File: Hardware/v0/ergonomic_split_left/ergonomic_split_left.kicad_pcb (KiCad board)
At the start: 2 copper layers, 189.3 x 173.4 mm, 96 parts, among them J1 USB_C_Receptacle_USB2.0, J2 Right_Interface, J3 Conn_01x02_Male, J5 Conn_02x03_Odd_Even, SW1 SW_Push, SW10 L31, SW11 L41, SW12 L51, SW13 L02, SW14 L12, SW15 L22, SW16 L32, SW17 L42, SW18 L52, SW19 L03, SW2 L00, SW20 L13, SW21 L23, SW22 L33, SW23 L43, SW24 L53, SW25 L04, SW26 L14, SW27 L24, SW28 L34, SW29 L44, SW3 L10, SW30 L54, SW31 L05, SW32 L15, SW33 L25, SW34 L35, SW35 L55, SW36 L16, SW37 L36, SW38 L56, SW39 L06, SW4 L20, SW40 L_Encoder, SW5 L30, SW6 L40, SW7 L01, SW8 L11, SW9 L21, U1 SRV05-4, U2 PCAL9555AHF, U6 ATmega32U4-AU, U9 TCR2EF33, X2 KC2016K

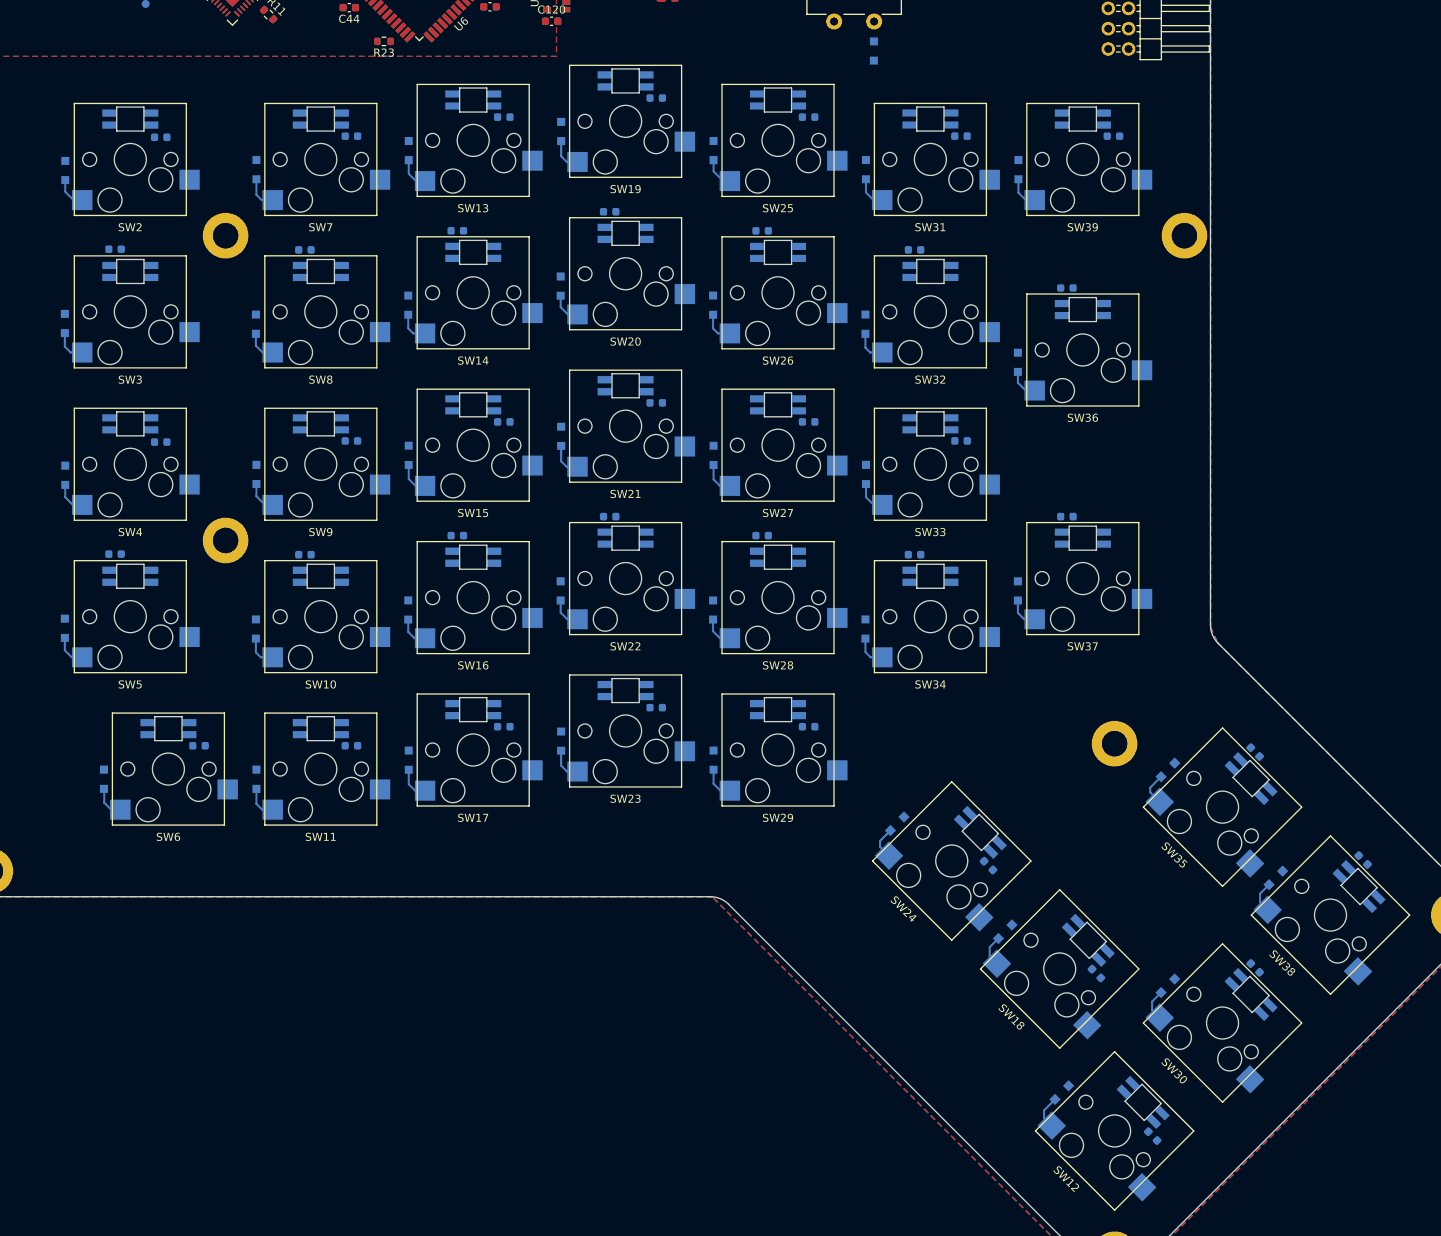
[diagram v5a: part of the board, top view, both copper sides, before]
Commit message: Switch matrix and LEDs prelim routing
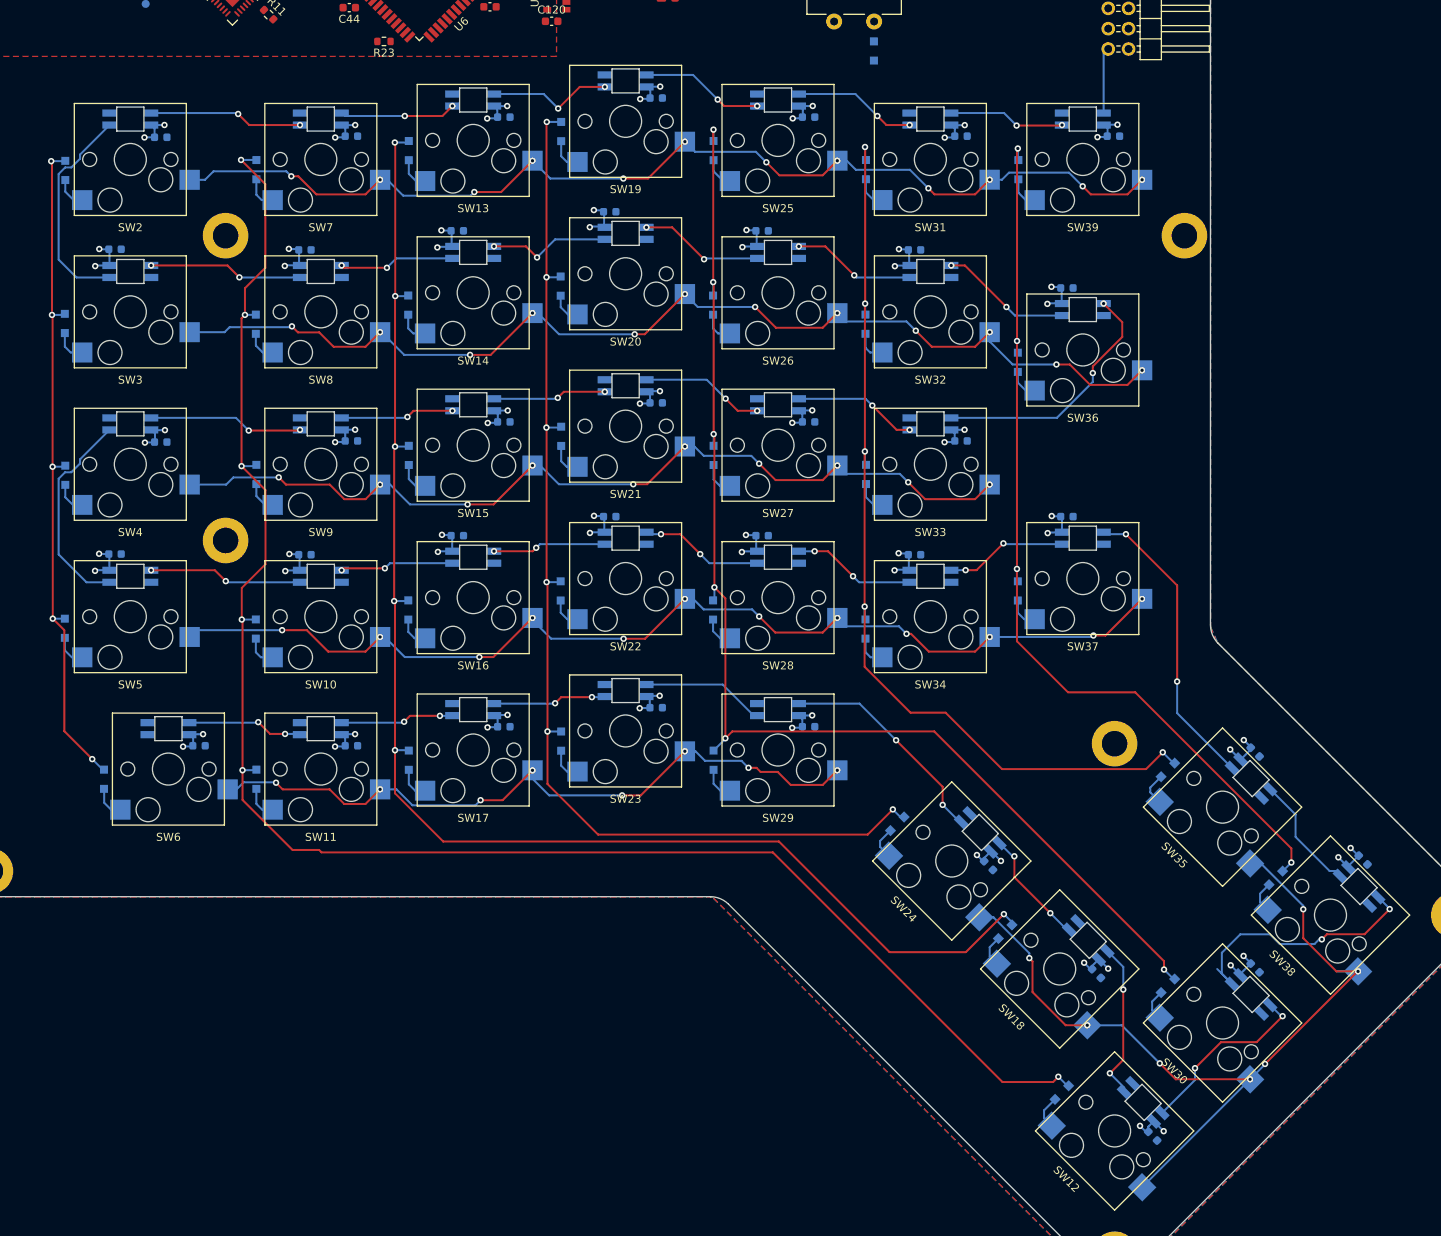
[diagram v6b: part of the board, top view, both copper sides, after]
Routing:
- net /IO Expander/COL[1]: track 0.00 -> 212.3 mm, vias 0 -> 6
- net +5V: track 0.00 -> 179.9 mm, vias 0 -> 76
- net /IO Expander/COL[2]: track 0.00 -> 178.3 mm, vias 0 -> 6
- net /IO Expander/COL[4]: track 0.00 -> 155.1 mm, vias 0 -> 6
- net /IO Expander/COL[3]: track 0.00 -> 140.7 mm, vias 0 -> 6
- net /IO Expander/ROW[1]: track 0.00 -> 136.9 mm, vias 0 -> 12
- net /IO Expander/ROW[3]: track 0.00 -> 134.6 mm, vias 0 -> 12
- net /IO Expander/ROW[0]: track 0.00 -> 134.2 mm, vias 0 -> 12
- net /IO Expander/COL[5]: track 0.00 -> 116.9 mm, vias 0 -> 5
- net /IO Expander/COL[6]: track 0.00 -> 114.5 mm, vias 0 -> 4
- net /IO Expander/ROW[2]: track 0.00 -> 113.2 mm, vias 0 -> 10
- net /IO Expander/ROW[5]: track 0.00 -> 107.2 mm, vias 0 -> 7
- net /IO Expander/ROW[4]: track 0.00 -> 87.8 mm, vias 0 -> 8
- net /IO Expander/COL[0]: track 0.00 -> 85.5 mm, vias 0 -> 5
- net /Switch Matrix/RGB_L55: track 0.00 -> 37.6 mm, vias 0 -> 2
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
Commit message: Prelim routing done
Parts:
- FB1, FB2, R1, R2, R22: moved to B.Cu
- moved SW1 59.8 mm to (99.0, 63.5), turned to 180 degrees
- moved R22 54.4 mm to (100.3, 66.2), turned to 0 degrees
- moved D194 50.1 mm to (140.4, 58.6), turned to 90 degrees
- moved R3 48.5 mm to (138.8, 58.6), turned to 270 degrees
- moved H5 22.0 mm to (168.5, 58.8)
- moved FB2 16.7 mm to (149.3, 62.0)
- moved FB1 5.84 mm to (162.0, 62.4)
- moved R1 5.00 mm to (148.6, 59.0), turned to 0 degrees
- moved TP2 4.91 mm to (92.2, 65.9)
- moved R2 4.77 mm to (158.6, 64.6)
- moved R5 4.49 mm to (149.4, 63.7)
- moved U1 4.37 mm to (155.7, 64.8), turned to 0 degrees
- moved J1 4.03 mm to (158.5, 61.7)
- moved C2 3.83 mm to (159.2, 63.7), turned to 0 degrees
- moved L1 3.73 mm to (153.5, 64.5)
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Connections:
- U1 pad 3: /USB_UPSTREAM/CD+ -> /USB_UPSTREAM/CD-
- U1 pad 4: /USB_UPSTREAM/CD- -> /USB_UPSTREAM/CD+
- U6 pad 38: /Switch Matrix/ENCODER_B_L -> /Right Interface/ENCODER_B_R
- U6 pad 39: /Switch Matrix/ENCODER_A_L -> /Right Interface/ENCODER_A_R
- U6 pad 40: /Right Interface/ENCODER_B_R -> /Switch Matrix/ENCODER_A_L
- U6 pad 41: /Right Interface/ENCODER_A_R -> /Switch Matrix/ENCODER_B_L
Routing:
- net /IO Expander/ROW[5]: track 107.2 -> 345.4 mm, vias 7 -> 11
- net /IO Expander/ROW[4]: track 87.8 -> 225.8 mm, vias 8 -> 10
- net /Switch Matrix/RGB_DIN: track 0.00 -> 130.9 mm, vias 0 -> 3
- net /IO Expander/SCL: track 0.00 -> 129.3 mm, vias 0 -> 1
- net /IO Expander/SDA: track 0.00 -> 124.9 mm, vias 0 -> 1
- net /IO Expander/ROW[3]: track 134.6 -> 256.3 mm, vias 12 -> 14
- net /IO Expander/COL[6]: track 114.5 -> 227.0 mm, vias 4 -> 8
- net /IO Expander/ROW[2]: track 113.2 -> 220.7 mm, vias 10 -> 12
- net /IO Expander/ROW[1]: track 136.9 -> 229.3 mm, vias 12 -> 14
- net /Right Interface/ENCODER_B_R: track 0.00 -> 89.0 mm, vias 0 -> 1
- net /IO Expander/COL[5]: track 116.9 -> 202.6 mm, vias 5 -> 8
- net /Right Interface/ENCODER_A_R: track 0.00 -> 85.5 mm, vias 0 -> 1
- net /IO Expander/ROW[6]: track 0.00 -> 84.5 mm, vias 0 -> 3
- net /IO Expander/ROW[0]: track 134.2 -> 209.9 mm, vias 12 -> 14
- net /IO Expander/COL[4]: track 155.1 -> 220.9 mm, vias 6 -> 8
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
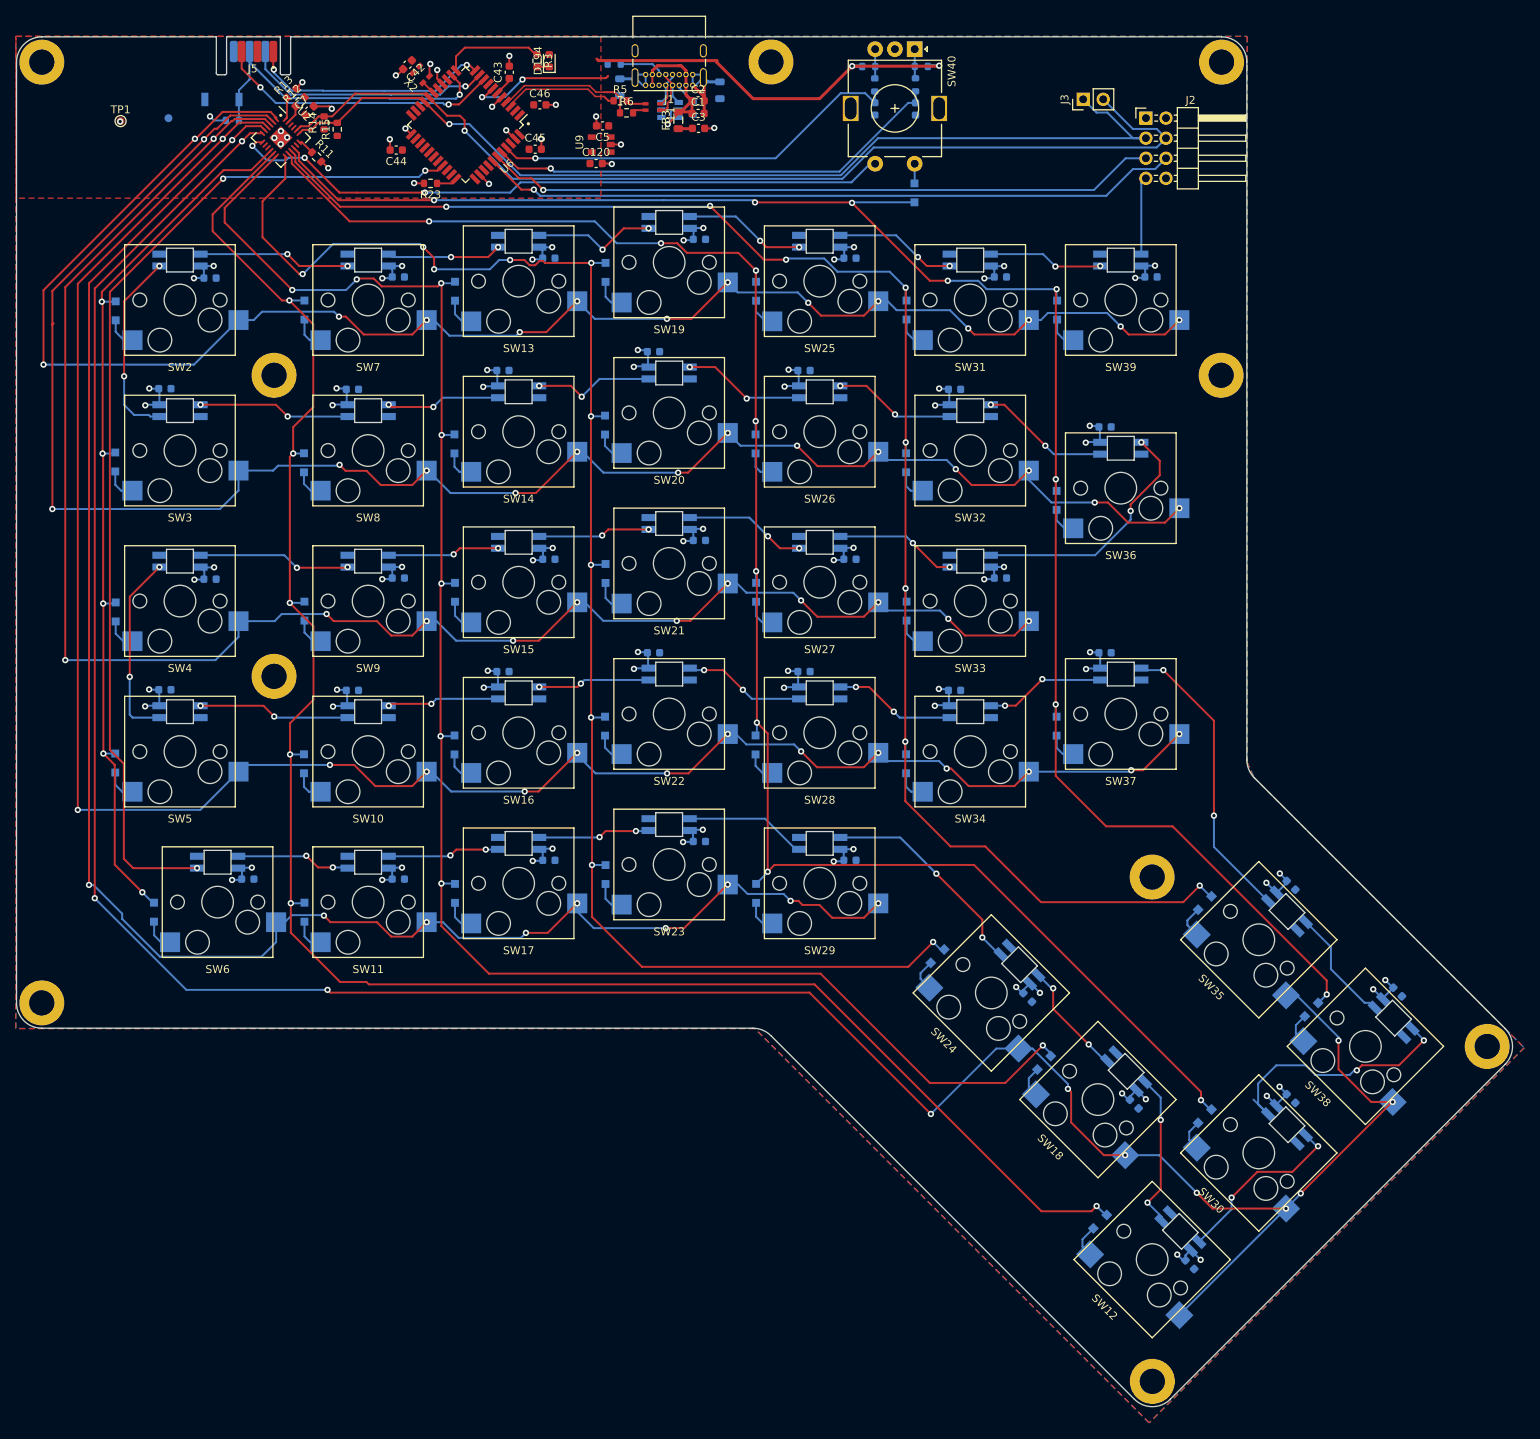
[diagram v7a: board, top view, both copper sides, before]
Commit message: Moving board edges in to 0.1in from keyswitches
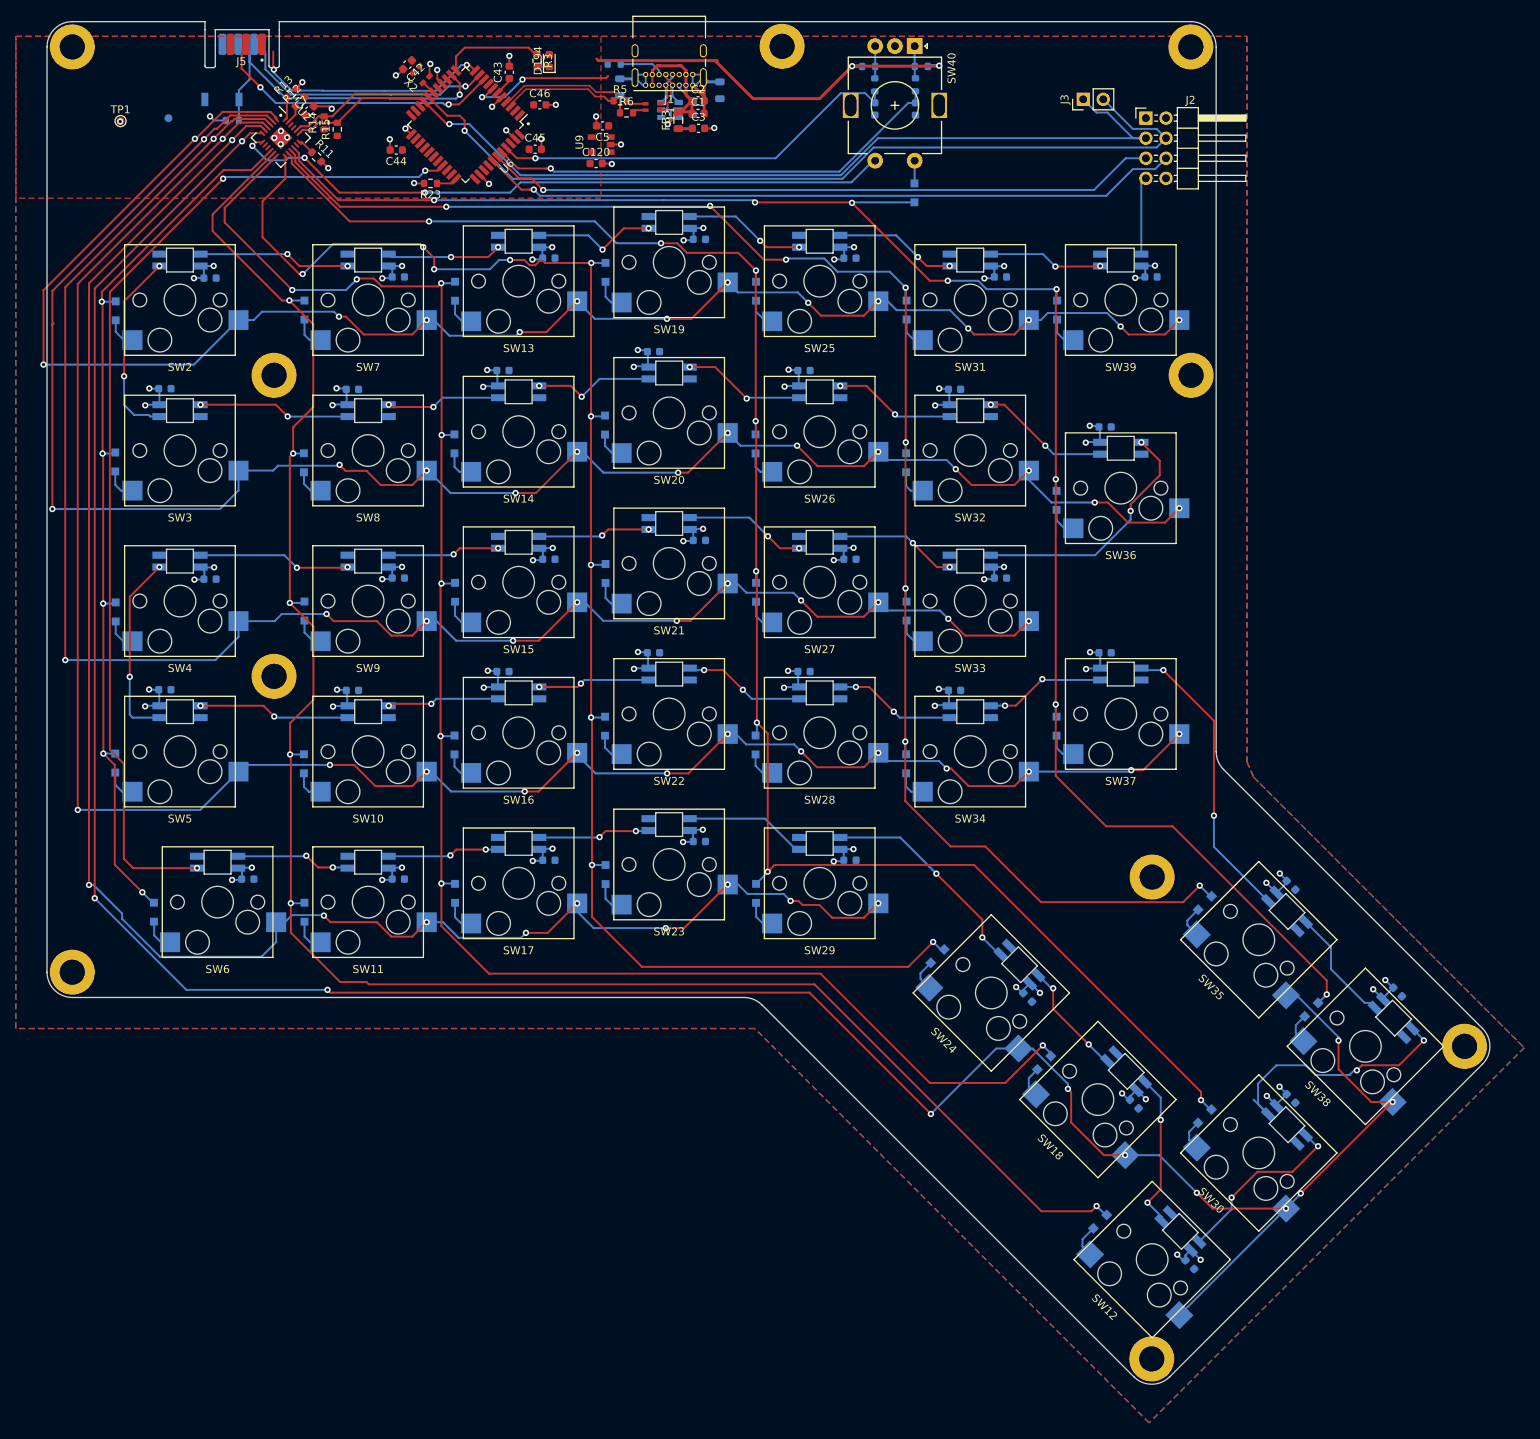
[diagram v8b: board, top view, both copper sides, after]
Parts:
- moved H2 5.48 mm to (80.0, 174.0)
- moved H8 4.34 mm to (221.6, 56.9)
- moved H1 4.31 mm to (80.0, 56.9)
- moved H9 3.80 mm to (221.6, 98.4)
- moved H6 2.87 mm to (256.2, 183.3)
- moved H3 2.84 mm to (216.6, 222.9)
- moved H5 2.43 mm to (169.9, 56.8)
- moved J5 1.70 mm to (104.0, 56.5)
- moved SW40 0.38 mm to (186.6, 56.8)
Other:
- board size 189.3 x 173.4 mm -> 182.6 x 172.4 mm
